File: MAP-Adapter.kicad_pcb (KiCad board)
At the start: 2 copper layers, 12 x 9 mm, 2 parts, among them J1 CONN_3, U6 MPXH6400AC6

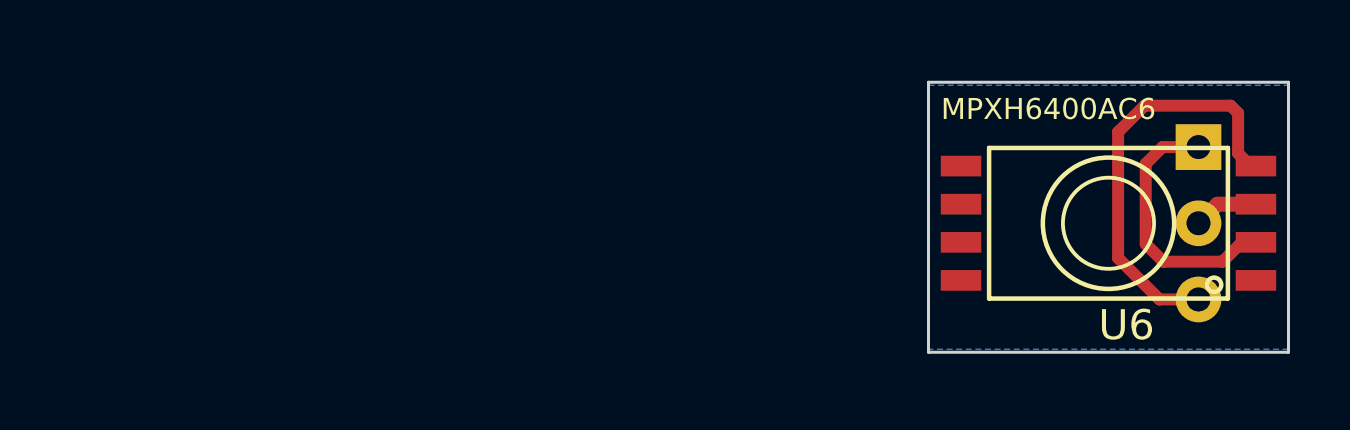
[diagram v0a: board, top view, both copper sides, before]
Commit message: Moved the alternate design to the main directory.
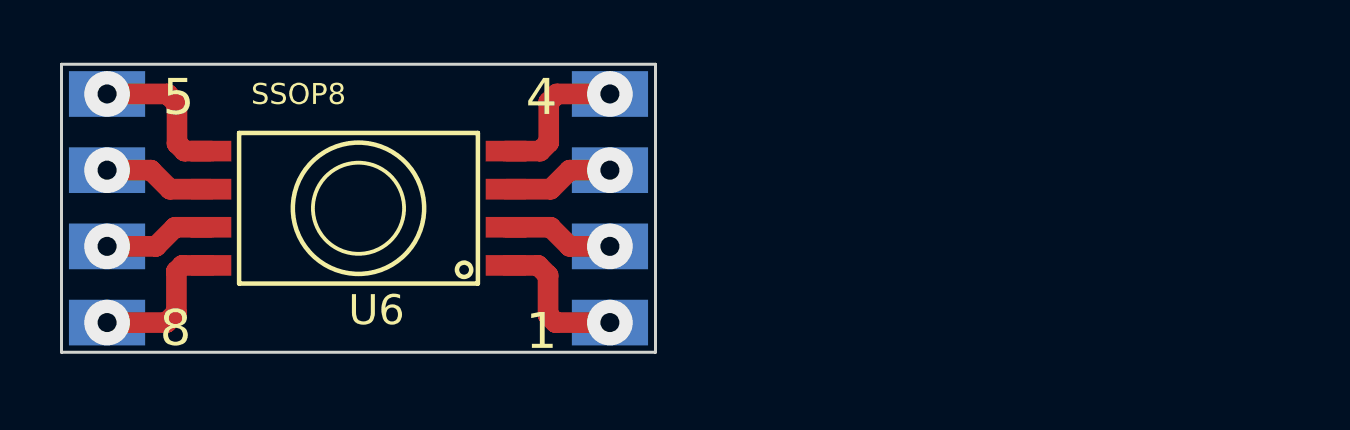
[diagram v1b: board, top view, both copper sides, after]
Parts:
- removed J1: CONN_3, PIN_ARRAY_3X1
- added U1: SOP8, 8-SOP, B.Cu at (216.4, 150.5)
- U6: value MPXH6400AC6 -> SSOP8
- moved U6 25.0 mm to (216.4, 150.5)
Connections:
- U6 pad 1: (no net) -> /Pin1
- U6 pad 5: (no net) -> /Pin5
- U6 pad 6: (no net) -> /Pin6
- U6 pad 7: (no net) -> /Pin7
- U6 pad 8: (no net) -> /Pin8
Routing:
- net /MAP: track 14.0 -> 5.05 mm, vias 0 -> 1
- net /5Vdc: track 8.85 -> 3.73 mm, vias 0 -> 1
- net /Pin8: track 0.00 -> 5.06 mm, vias 0 -> 1
- net /Pin5: track 0.00 -> 5.04 mm, vias 0 -> 1
- net /Pin1: track 0.00 -> 5.03 mm, vias 0 -> 1
- net /Pin7: track 0.00 -> 3.73 mm, vias 0 -> 1
- net /Pin6: track 0.00 -> 3.73 mm, vias 0 -> 1
- net /GND: track 2.18 -> 3.73 mm, vias 0 -> 1
- removed copper zone on B.Cu, net /GND
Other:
- board size 12 x 9 mm -> 19.8 x 9.6 mm
- net class SSOP: trace_width 0.4 -> 0.69; via_dia 0.889 -> 1.524; via_drill 0.635 -> 1.2
- board text added: "1"
- board text added: "4"
- board text added: "5"
- board text added: "8"

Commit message: Added git hash to KiCAD files and created the Gerber files.
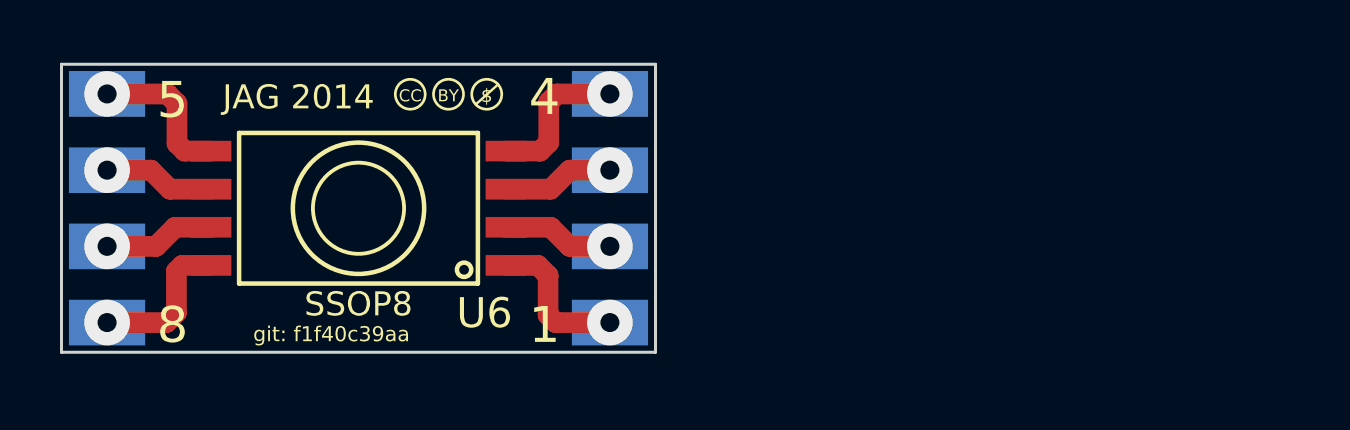
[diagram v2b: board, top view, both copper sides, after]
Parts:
- added CC-logo: G**, CC-BY-NC-logo, F.Cu at (219.4, 146.7)
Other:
- board text added: "JAG 2014"
- board text added: "git: f1f40c39aa"
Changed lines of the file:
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@@
     (links 8)
     (no_connects 0)
-    (area 197.100001 140.650001 234.835715 160.6)
+    (area 197.614287 141.450001 236.635715 159.7)
     (thickness 1.6)
-    (drawings 12)
+    (drawings 14)
     (tracks 48)
     (zones 0)
-    (modules 2)
+    (modules 3)
     (nets 9)
   )
   (page A3)
+  (title_block
+    (title MAP-Adapter)
+    (rev 0.1-alpha)
+    (company "git: f1f40c39aa")
+  )
   (layers
     (15 F.Cu signal)
@@
     (visible_elements 7FFFFFFF)
     (pcbplotparams
-      (layerselection 3178497)
+      (layerselection 284196865)
       (usegerberextensions true)
       (excludeedgelayer true)
@@
       (drillshape 0)
       (scaleselection 1)
-      (outputdirectory Gerber/Adapter/))
+      (outputdirectory Gerber/))
   )
   (net 0 "")
@@
   (module SSOP-8-Freescale (layer F.Cu)
     (at 216.4 150.5)
-    (fp_text reference U6 (at 0.6 3.4) (layer F.SilkS)
-      (effects (font (size 1 1) (thickness 0.1016)))
-    )
-    (fp_text value SSOP8 (at -2 -3.8) (layer F.SilkS)
-      (effects (font (size 0.7 0.7) (thickness 0.1016)))
+    (fp_text reference U6 (at 4.2 3.5) (layer F.SilkS)
+      (effects (font (size 1 1) (thickness 0.2)))
+    )
+    (fp_text value SSOP8 (at 0 3.2) (layer F.SilkS)
+      (effects (font (size 0.8 0.8) (thickness 0.18)))
     )
     (fp_circle (center 0 0) (end 2.15 0.41) (layer F.SilkS) (width 0.15))
@@
   (module 8-SOP (layer B.Cu)
     (at 216.4 150.5 180)
-    (fp_text reference U1 (at -0.09906 2.6797 180) (layer B.SilkS)
-      (effects (font (size 1.524 1.524) (thickness 0.3048)) (justify mirror))
-    )
-    (fp_text value SOP8 (at 0.07874 -3.63982 180) (layer B.SilkS)
-      (effects (font (size 1.524 1.524) (thickness 0.3048)) (justify mirror))
+    (fp_text reference U1 (at -4.1 -3.5 180) (layer B.SilkS)
+      (effects (font (size 1 1) (thickness 0.2)) (justify mirror))
+    )
+    (fp_text value SOP8 (at 0 -3.2 180) (layer B.SilkS)
+      (effects (font (size 0.8 0.8) (thickness 0.18)) (justify mirror))
     )
     (fp_circle (center 0 0) (end 1.51892 0) (layer B.SilkS) (width 0.127))
@@
     )
   )
+  (module CC-BY-NC-logo (layer F.Cu)
+    (at 219.4 146.7)
+    (fp_text reference CC-logo (at -0.1 -0.725) (layer F.SilkS) hide
+      (effects (font (size 0.2 0.2) (thickness 0.05)))
+    )
+    (fp_text value G** (at 0.025 0.75) (layer F.SilkS) hide
+      (effects (font (size 0.2 0.2) (thickness 0.05)))
+    )
+    (fp_line (start 1.65 -0.325) (end 0.925 0.325) (layer F.SilkS) (width 0.08))
+    (fp_circle (center 1.275 0) (end 1.275 -0.5) (layer F.SilkS) (width 0.09))
+    (fp_circle (center -1.275 0) (end -0.8 -0.15) (layer F.SilkS) (width 0.09))
+    (fp_text user CC (at -1.275 0.05) (layer F.SilkS)
+      (effects (font (size 0.4 0.4) (thickness 0.09)))
+    )
+    (fp_circle (center 0 0) (end 0.4 -0.3) (layer F.SilkS) (width 0.09))
+    (fp_text user $ (at 1.275 0.05) (layer F.SilkS)
+      (effects (font (size 0.45 0.45) (thickness 0.09)))
+    )
+    (fp_text user BY (at -0.01 0.05) (layer F.SilkS)
+      (effects (font (size 0.4 0.4) (thickness 0.09)))
+    )
+  )
+  (gr_text "JAG 2014" (at 214.4 146.8) (layer F.SilkS)
+    (effects (font (size 0.8 0.8) (thickness 0.15)))
+  )
+  (gr_text "git: f1f40c39aa" (at 215.5 154.7) (layer F.SilkS)
+    (effects (font (size 0.5 0.5) (thickness 0.1)))
+  )
   (dimension 9.6 (width 0.3) (layer Eco1.User)
     (gr_text "0.3780 in" (at 230.95 150.5 90) (layer Eco1.User)
@@
   (gr_line (start 226.3 145.7) (end 226.3 155.3) (angle 90) (layer Edge.Cuts) (width 0.1))
   (gr_line (start 206.5 145.7) (end 226.3 145.7) (angle 90) (layer Edge.Cuts) (width 0.1))
-  (gr_text 8 (at 210.3 154.5) (layer F.SilkS)
+  (gr_text 8 (at 210.2 154.4) (layer F.SilkS)
     (effects (font (size 1.2 1.2) (thickness 0.18)))
   )
-  (gr_text 5 (at 210.4 146.8) (layer F.SilkS)
+  (gr_text 5 (at 210.2 146.9) (layer F.SilkS)
     (effects (font (size 1.2 1.2) (thickness 0.18)))
   )
-  (gr_text 4 (at 222.5 146.8) (layer F.SilkS)
+  (gr_text 4 (at 222.6 146.8) (layer F.SilkS)
     (effects (font (size 1.2 1.2) (thickness 0.18)))
   )
-  (gr_text 1 (at 222.5 154.6) (layer F.SilkS)
+  (gr_text 1 (at 222.6 154.4) (layer F.SilkS)
     (effects (font (size 1.2 1.2) (thickness 0.18)))
   )
